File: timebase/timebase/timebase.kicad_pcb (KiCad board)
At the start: 2 copper layers, 85.3 x 76.5 mm, 57 parts, among them J402 Jack-DC, J404 Jack-DC, J8 Conn_Coaxial, J9 Conn_Coaxial, U401 LM358, U402 LM358, U403 LM358

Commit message: if and log amp routing and 3d model
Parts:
- J8, J9: footprint SnapEDA Library:TE_5-1634503-1 -> timebase:TE_5-1634503-1

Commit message: timebase updates
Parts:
- C401: footprint Capacitor_THT:C_Radial_D4.0mm_H5.0mm_P1.50mm -> Capacitor_THT:CP_Radial_D8.0mm_P3.50mm
- C402, C403, C404, C405, C406: footprint Capacitor_THT:CP_Axial_L11.0mm_D6.0mm_P18.00mm_Horizontal -> Capacitor_THT:CP_Radial_D8.0mm_P3.50mm
- H1, H2, H3, H4: footprint MountingHole:MountingHole_2.7mm_M2.5_DIN965_Pad_TopOnly -> MountingHole:MountingHole_3.2mm_M3
- J402, J404: footprint SnapEDA Library:CUI_PJ-007 -> timebase:691137710002
- J8, J9: footprint timebase:TE_5-1634503-1 -> timebase:MOLEX_73391-0060
- R3, R4, R5, R6: footprint Connector_Wire:SolderWire-0.127sqmm_1x03_P3.7mm_D0.48mm_OD1mm -> Connector_Wire:SolderWire-0.25sqmm_1x03_P4.2mm_D0.65mm_OD1.7mm
- U401, U402, U403: footprint SnapEDA Library:DIP794W45P254L959H508Q8 -> timebase:DIP794W45P254L959H508Q8
- moved J404 8.63 mm to (108.2, 75.9)
- moved J402 8.35 mm to (108.2, 84.8)
- moved C406 7.73 mm to (152.8, 77.2)
- moved R3 6.94 mm to (114.2, 129.5)
- moved C402 6.70 mm to (150.6, 99.8)
- moved C405 3.98 mm to (142.6, 126.5)
- moved C404 3.67 mm to (120.0, 126.2)
- moved C403 3.42 mm to (132.0, 98.8)
- moved R5 2.90 mm to (99.6, 117.7)
- moved R4 2.45 mm to (99.8, 113.0)
- moved C401 1.48 mm to (109.0, 106.4)
- moved R6 0.36 mm to (100.1, 91.6)
- moved U403 0.25 mm to (131.3, 110.2)
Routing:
- net GND: track 308.7 -> 249.4 mm
- net Net-(C404-Pad2): track 49.8 -> 38.0 mm
- net V-15: track 156.9 -> 145.5 mm
- net Net-(C402-Pad1): track 36.3 -> 43.0 mm
- net Net-(C403-Pad1): track 74.8 -> 80.5 mm
- net V+15: track 57.0 -> 61.7 mm
- net Net-(C401-Pad2): track 57.2 -> 61.6 mm
- net Net-(C406-Pad1): track 54.2 -> 50.6 mm
- net Net-(R426-Pad2): track 48.5 -> 52.2 mm
- net Net-(R417-Pad1): track 18.2 -> 20.5 mm
- net Net-(R418-Pad1): track 19.7 -> 21.9 mm
- net Net-(C405-Pad2): track 35.6 -> 33.9 mm
- net Net-(R421-Pad2): track 35.0 -> 36.0 mm
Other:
- board text added: "+15"
- board text added: "-15"
- board text added: "Fine Tune"
- board text added: "Span"
- board text added: "Spectrum Analyzer Time Base Rev 1.0"
- board text added: "Sweep Rate"
- board text added: "Tune"

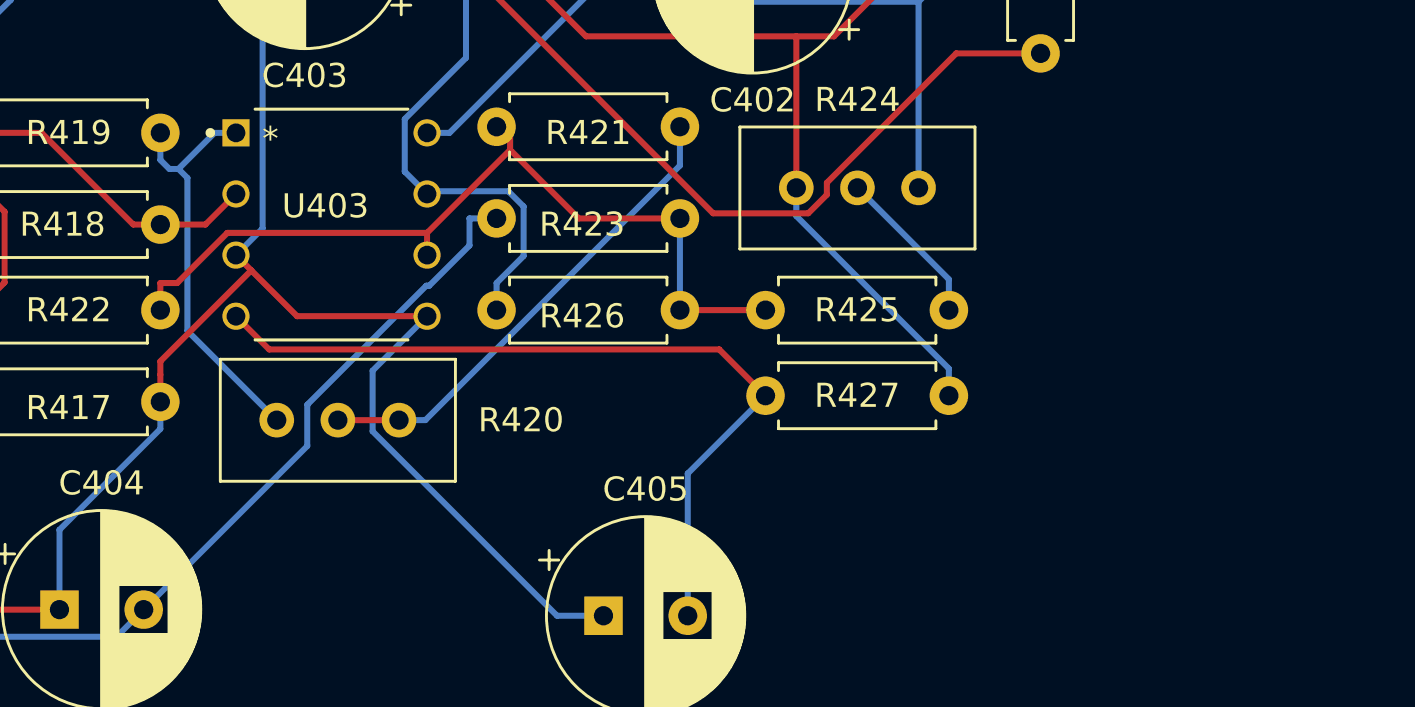
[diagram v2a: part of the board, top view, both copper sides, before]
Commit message: some improvements to timebase and if log amp
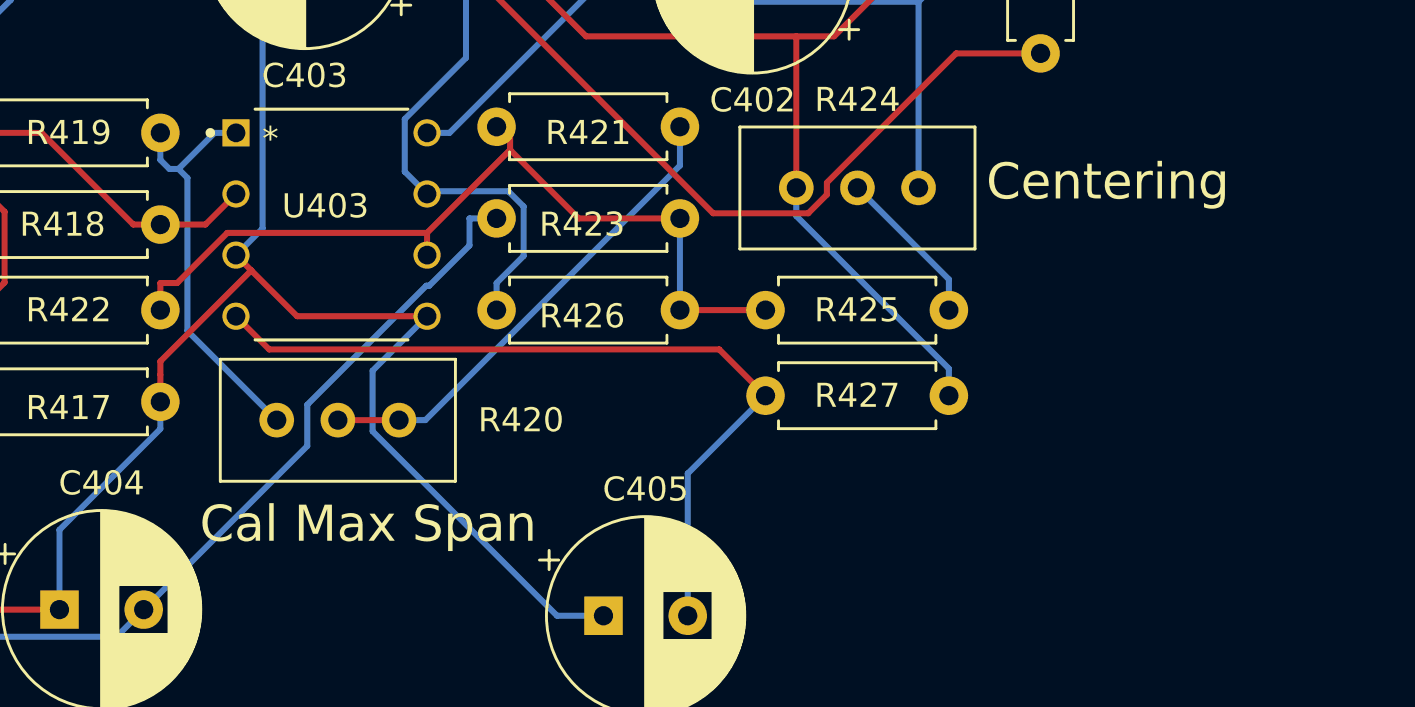
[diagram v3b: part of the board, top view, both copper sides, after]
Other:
- board text added: "Cal Max Span"
- board text added: "Centering"
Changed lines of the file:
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@@
   )
   (gr_rect (start 97.028 61.976) (end 182.372 138.43) (layer "Edge.Cuts") (width 0.1) (fill none))
+  (gr_text "Centering" (at 163.576 108.458) (layer "F.SilkS")
+    (effects (font (size 1.5 1.5) (thickness 0.3)))
+  )
+  (gr_text "Cal Max Span" (at 132.842 122.682) (layer "F.SilkS")
+    (effects (font (size 1.5 1.5) (thickness 0.3)))
+  )
   (gr_text "Spectrum Analyzer Time Base Rev 1.0" (at 179.07 99.314 90) (layer "F.SilkS")
     (effects (font (size 1.5 1.5) (thickness 0.3)))

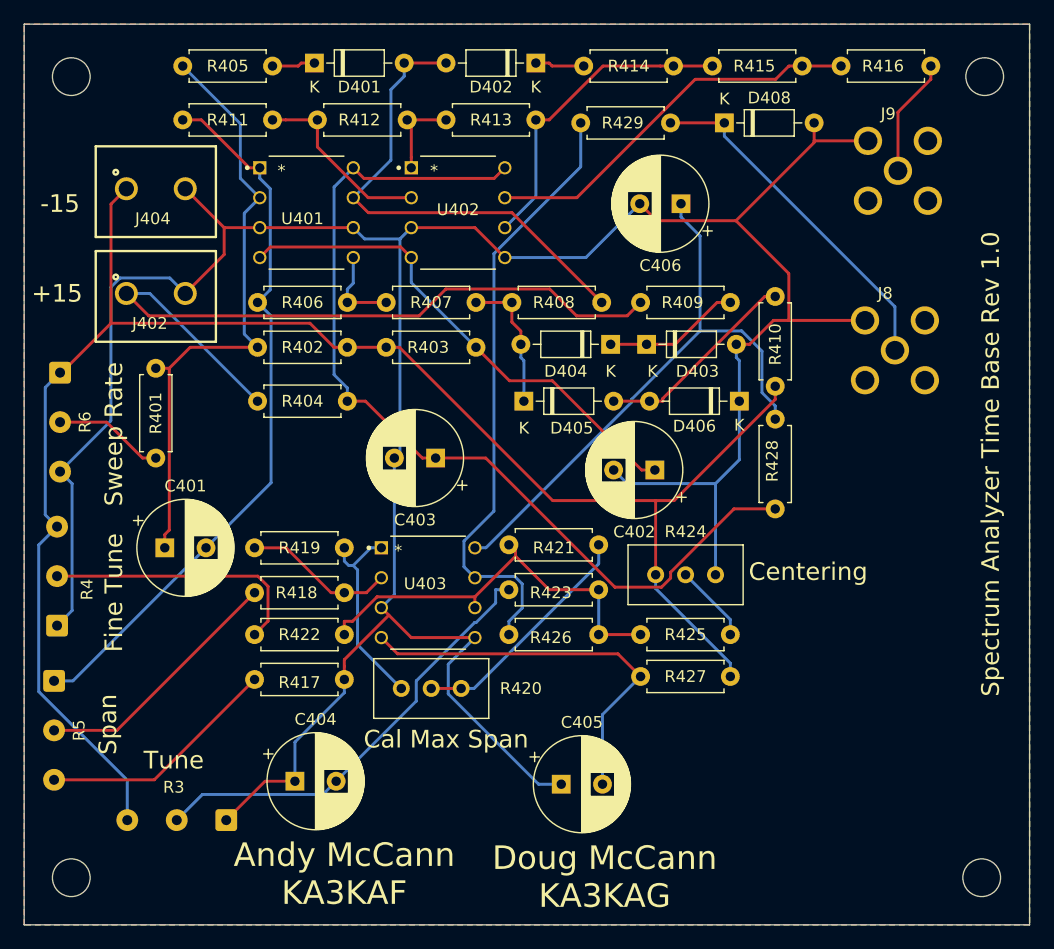
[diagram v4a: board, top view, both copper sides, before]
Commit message: Update to timebase and 2lo gerbers
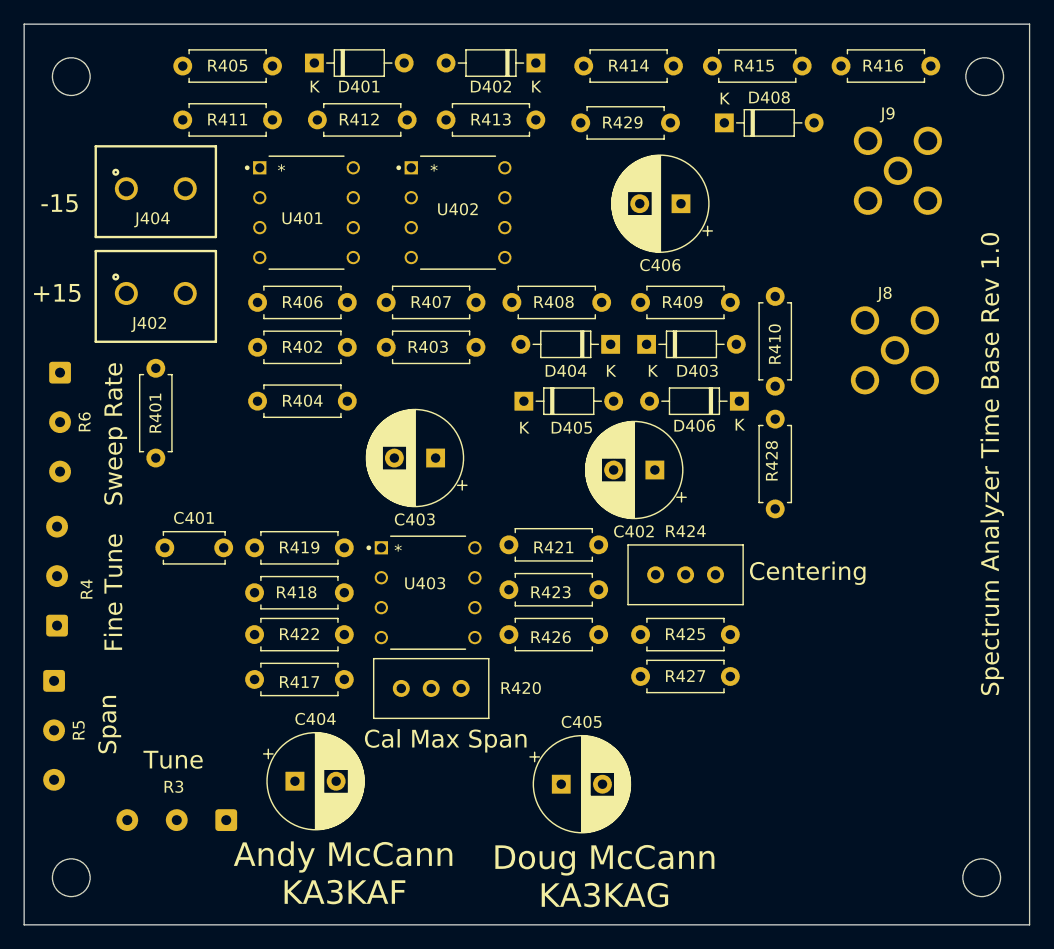
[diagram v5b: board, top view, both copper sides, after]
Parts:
- C401: footprint Capacitor_THT:CP_Radial_D8.0mm_P3.50mm -> Capacitor_THT:C_Disc_D5.0mm_W2.5mm_P5.00mm
- H1, H2, H3, H4: value MountingHole_Pad -> type="R" model="MountingHole_Pad" lib=""
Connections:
- J402 pad 1: V+15 -> unconnected-(J402-Pad1)
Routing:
- net GND: track 249.4 -> 0.00 mm
- net V-15: track 145.5 -> 0.00 mm
- net Net-(#FLG0401-pwr): track 80.5 -> 0.00 mm
- net V+15: track 61.7 -> 0.00 mm
- net Net-(C401-Pad2): track 61.6 -> 0.00 mm
- net Net-(U401A--): track 52.4 -> 0.00 mm
- net Net-(R426-Pad2): track 52.2 -> 0.00 mm
- net Net-(#FLG0403-pwr): track 50.6 -> 0.00 mm
- net Net-(#FLG0402-pwr): track 43.0 -> 0.00 mm
- net Net-(D401-A): track 41.5 -> 0.00 mm
- net Net-(C404-Pad2): track 38.0 -> 0.00 mm
- net Net-(U403B--): track 36.0 -> 0.00 mm
- net Net-(#FLG0404-pwr): track 33.9 -> 0.00 mm
- net Net-(R415-Pad2): track 33.2 -> 0.00 mm
- net VCO_Out: track 29.9 -> 0.00 mm
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- removed copper zone on B.Cu, net GND
- removed copper zone on F.Cu, net GND

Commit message: timebase rev 1 - fixes silkscreen
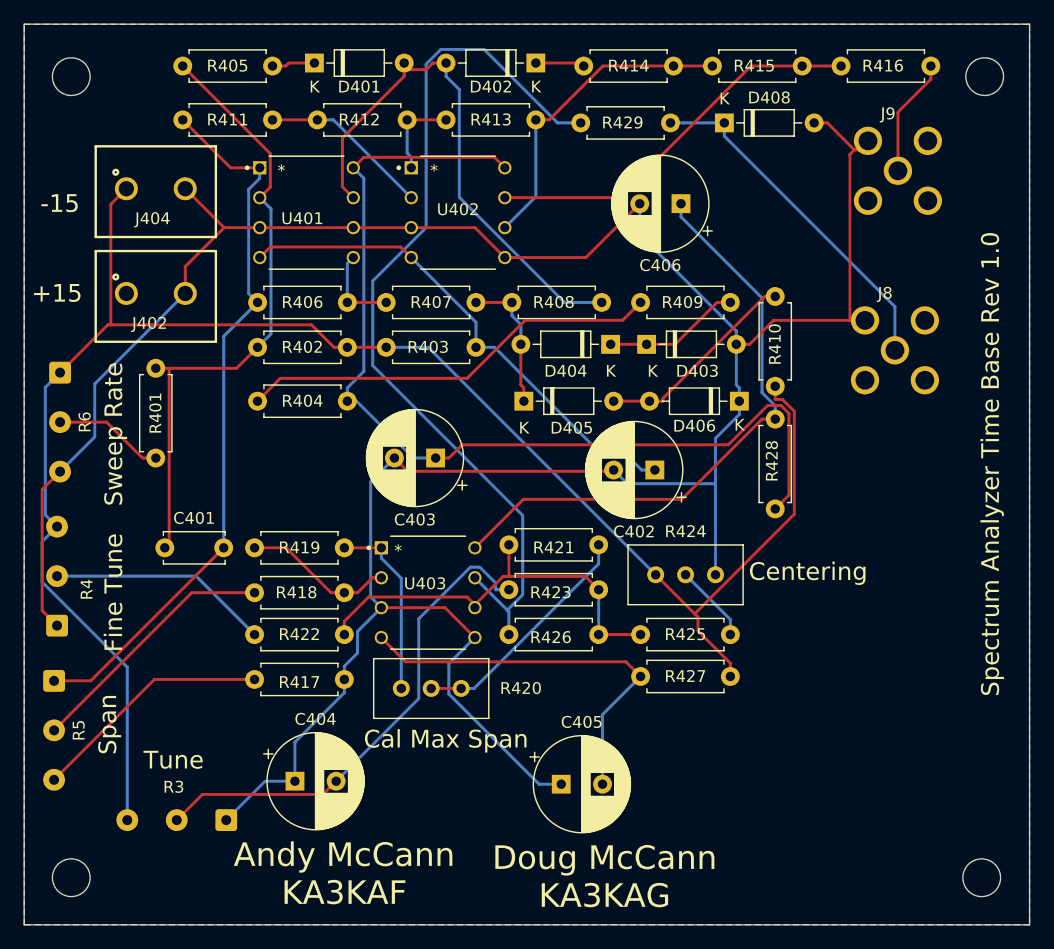
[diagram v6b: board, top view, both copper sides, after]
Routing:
- net GND: track 0.00 -> 246.2 mm
- net V-15: track 0.00 -> 150.7 mm
- net Net-(#FLG0401-pwr): track 0.00 -> 84.9 mm
- net Net-(R426-Pad2): track 0.00 -> 76.3 mm
- net Net-(C401-Pad2): track 0.00 -> 61.4 mm
- net Net-(U401A--): track 0.00 -> 53.0 mm
- net Net-(#FLG0403-pwr): track 0.00 -> 51.6 mm
- net Net-(D401-A): track 0.00 -> 45.4 mm
- net Net-(#FLG0402-pwr): track 0.00 -> 43.0 mm
- net Net-(C404-Pad2): track 0.00 -> 42.2 mm
- net V+15: track 0.00 -> 36.0 mm
- net Net-(U403B--): track 0.00 -> 35.6 mm
- net Net-(#FLG0404-pwr): track 0.00 -> 33.9 mm
- net Net-(R415-Pad2): track 0.00 -> 33.2 mm
- net VCO_Out: track 0.00 -> 29.9 mm
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- added copper zone on B.Cu, net GND
- added copper zone on F.Cu, net GND
